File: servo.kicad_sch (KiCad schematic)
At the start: 31 parts, among them J20 Conn_04x03_Servo, J22 Conn_04x03_Servo, J23 Conn_04x03_Servo, J24 Conn_04x03_Servo, J25 Conn_02x02_Odd_Even, U14 PCA9685BS

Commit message: sch: erc
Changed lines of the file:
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@@
 	(paper "A4")
 	(junction
-		(at 182.88 130.81)
-		(diameter 0)
-		(color 0 0 0 0)
-	)
-	(junction
 		(at 179.07 130.81)
 		(diameter 0)
@@
 	(wire
 		(pts
-			(xy 182.88 123.19) (xy 182.88 128.27)
-		)
-		(stroke
-			(width 0)
-			(type default)
-		)
-	)
-	(wire
-		(pts
 			(xy 143.51 86.36) (xy 138.43 86.36)
 		)
@@
 	(wire
 		(pts
-			(xy 195.58 123.19) (xy 195.58 128.27)
-		)
-		(stroke
-			(width 0)
-			(type default)
-		)
-	)
-	(wire
-		(pts
 			(xy 143.51 88.9) (xy 138.43 88.9)
 		)
@@
 	)
 	(symbol
-		(lib_id "power:PWR_FLAG")
-		(at 195.58 123.19 0)
-		(unit 1)
-		(exclude_from_sim no)
-		(in_bom yes)
-		(on_board yes)
-		(dnp no)
-		(fields_autoplaced yes)
-		(property "Reference" "#FLG07"
-			(at 195.58 121.285 0)
-			(effects
-				(font
-					(size 1.27 1.27)
-				)
-				(hide yes)
-			)
-		)
-		(property "Value" "PWR_FLAG"
-			(at 195.58 118.11 0)
-			(effects
-				(font
-					(size 1.27 1.27)
-				)
-			)
-		)
-		(property "Footprint" ""
-			(at 195.58 123.19 0)
-			(effects
-				(font
-					(size 1.27 1.27)
-				)
-				(hide yes)
-			)
-		)
-		(property "Datasheet" "~"
-			(at 195.58 123.19 0)
-			(effects
-				(font
-					(size 1.27 1.27)
-				)
-				(hide yes)
-			)
-		)
-		(property "Description" "Special symbol for telling ERC where power comes from"
-			(at 195.58 123.19 0)
-			(effects
-				(font
-					(size 1.27 1.27)
-				)
-				(hide yes)
-			)
-		)
-		(pin "1"
-		)
-		(instances
-			(project "P2 Kevinbot Board"
-				(path "/362ca48c-0b77-4943-b8b3-fc15ab97f30d/7b0b1465-76e8-4550-9366-259d540e6b80/f1106b7e-a892-4542-9aa4-e84e85953c9f"
-					(reference "#FLG07")
-					(unit 1)
-				)
-			)
-		)
-	)
-	(symbol
 		(lib_id "Connector_Generic:Conn_02x02_Odd_Even")
 		(at 187.96 128.27 0)
@@
 	(symbol
 		(lib_id "power:PWR_FLAG")
-		(at 182.88 130.81 180)
-		(unit 1)
-		(exclude_from_sim no)
-		(in_bom yes)
-		(on_board yes)
-		(dnp no)
-		(fields_autoplaced yes)
-		(property "Reference" "#FLG06"
-			(at 182.88 132.715 0)
-			(effects
-				(font
-					(size 1.27 1.27)
-				)
-				(hide yes)
-			)
-		)
-		(property "Value" "PWR_FLAG"
-			(at 182.88 135.89 0)
-			(effects
-				(font
-					(size 1.27 1.27)
-				)
-			)
-		)
-		(property "Footprint" ""
-			(at 182.88 130.81 0)
-			(effects
-				(font
-					(size 1.27 1.27)
-				)
-				(hide yes)
-			)
-		)
-		(property "Datasheet" "~"
-			(at 182.88 130.81 0)
-			(effects
-				(font
-					(size 1.27 1.27)
-				)
-				(hide yes)
-			)
-		)
-		(property "Description" "Special symbol for telling ERC where power comes from"
-			(at 182.88 130.81 0)
-			(effects
-				(font
-					(size 1.27 1.27)
-				)
-				(hide yes)
-			)
-		)
-		(pin "1"
-		)
-		(instances
-			(project "P2 Kevinbot Board"
-				(path "/362ca48c-0b77-4943-b8b3-fc15ab97f30d/7b0b1465-76e8-4550-9366-259d540e6b80/f1106b7e-a892-4542-9aa4-e84e85953c9f"
-					(reference "#FLG06")
-					(unit 1)
-				)
-			)
-		)
-	)
-	(symbol
-		(lib_id "power:PWR_FLAG")
 		(at 195.58 130.81 180)
 		(unit 1)
@@
 					(unit 1)
 				)
-			)
-		)
-	)
-	(symbol
-		(lib_id "power:PWR_FLAG")
-		(at 182.88 123.19 0)
-		(unit 1)
-		(exclude_from_sim no)
-		(in_bom yes)
-		(on_board yes)
-		(dnp no)
-		(fields_autoplaced yes)
-		(property "Reference" "#FLG05"
-			(at 182.88 121.285 0)
-			(effects
-				(font
-					(size 1.27 1.27)
-				)
-				(hide yes)
-			)
-		)
-		(property "Value" "PWR_FLAG"
-			(at 182.88 118.11 0)
-			(effects
-				(font
-					(size 1.27 1.27)
-				)
-			)
-		)
-		(property "Footprint" ""
-			(at 182.88 123.19 0)
-			(effects
-				(font
-					(size 1.27 1.27)
-				)
-				(hide yes)
-			)
-		)
-		(property "Datasheet" "~"
-			(at 182.88 123.19 0)
-			(effects
-				(font
-					(size 1.27 1.27)
-				)
-				(hide yes)
-			)
-		)
-		(property "Description" "Special symbol for telling ERC where power comes from"
-			(at 182.88 123.19 0)
-			(effects
-				(font
-					(size 1.27 1.27)
-				)
-				(hide yes)
-			)
-		)
-		(pin "1"
-		)
-		(instances
-			(project "P2 Kevinbot Board"
-				(path "/362ca48c-0b77-4943-b8b3-fc15ab97f30d/7b0b1465-76e8-4550-9366-259d540e6b80/f1106b7e-a892-4542-9aa4-e84e85953c9f"
-					(reference "#FLG05")
-					(unit 1)
-				)

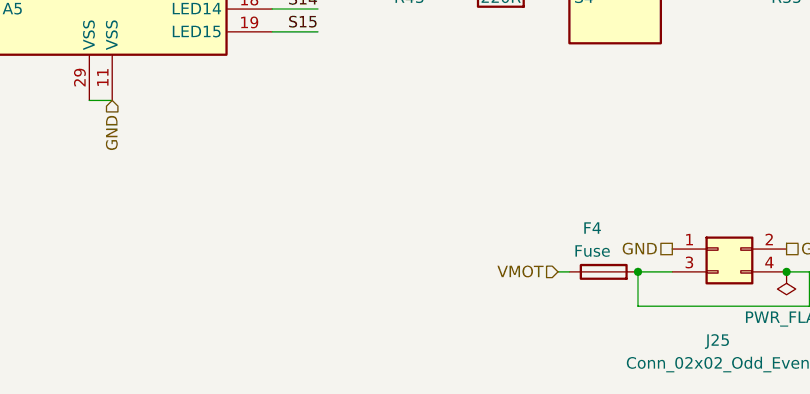
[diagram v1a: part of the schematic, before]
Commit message: Servo filtering, cleanup
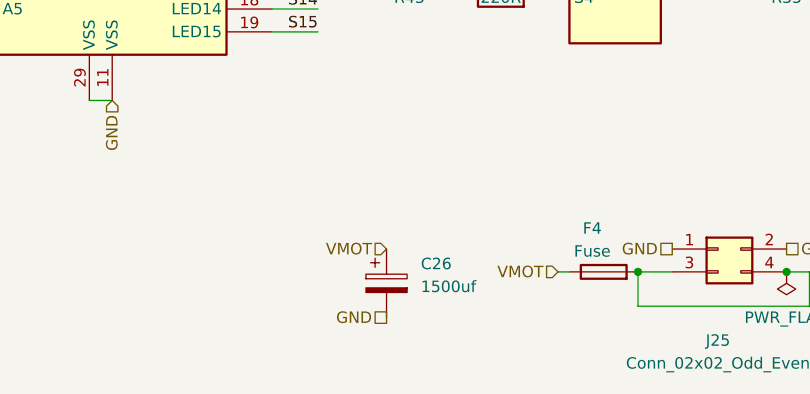
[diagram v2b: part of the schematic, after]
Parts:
- added C26: 1500uf, Capacitor_THT:CP_Radial_D8.0mm_P3.50mm, symbol Device:C_Polarized
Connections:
- net GND: now also C26.2
- net VMOT: now also C26.1
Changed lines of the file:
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@@
+		)
+	)
+	(hierarchical_label "VMOT"
+		(shape input)
+		(at 151.13 128.27 180)
+		(effects
+			(font
+				(size 1.27 1.27)
+			)
+			(justify right)
 		)
 	)
@@
 	)
 	(hierarchical_label "GND"
+		(shape passive)
+		(at 151.13 135.89 180)
+		(effects
+			(font
+				(size 1.27 1.27)
+			)
+			(justify right)
+		)
+	)
+	(hierarchical_label "GND"
 		(shape input)
 		(at 102.87 71.12 180)
@@
 					(unit 1)
 				)
+			)
+		)
+	)
+	(symbol
+		(lib_id "Device:C_Polarized")
+		(at 151.13 132.08 0)
+		(unit 1)
+		(exclude_from_sim no)
+		(in_bom yes)
+		(on_board yes)
+		(dnp no)
+		(fields_autoplaced yes)
+		(property "Reference" "C26"
+			(at 154.94 129.9209 0)
+			(effects
+				(font
+					(size 1.27 1.27)
+				)
+				(justify left)
+			)
+		)
+		(property "Value" "1500uf"
+			(at 154.94 132.4609 0)
+			(effects
+				(font
+					(size 1.27 1.27)
+				)
+				(justify left)
+			)
+		)
+		(property "Footprint" "Capacitor_THT:CP_Radial_D8.0mm_P3.50mm"
+			(at 152.0952 135.89 0)
+			(effects
+				(font
+					(size 1.27 1.27)
+				)
+				(hide yes)
+			)
+		)
+		(property "Datasheet" "https://connect.kemet.com:7667/gateway/IntelliData-ComponentDocumentation/1.0/download/datasheet/A750KS158M0JAAE014"
+			(at 151.13 132.08 0)
+			(effects
+				(font
+					(size 1.27 1.27)
+				)
+				(hide yes)
+			)
+		)
+		(property "Description" "Polarized capacitor"
+			(at 151.13 132.08 0)
+			(effects
+				(font
+					(size 1.27 1.27)
+				)
+				(hide yes)
+			)
+		)
+		(property "Part Number" "A750KS158M0JAAE014"
+			(at 151.13 132.08 0)
+			(effects
+				(font
+					(size 1.27 1.27)
+				)
+				(hide yes)
+			)
+		)
+		(pin "1"
+		)
+		(pin "2"
+		)
+		(instances
+			(project "P2 Kevinbot Board"
+				(path "/362ca48c-0b77-4943-b8b3-fc15ab97f30d/7b0b1465-76e8-4550-9366-259d540e6b80/f1106b7e-a892-4542-9aa4-e84e85953c9f"
+					(reference "C26")
+					(unit 1)
+				)
